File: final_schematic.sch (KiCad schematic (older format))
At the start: 50 parts, among them J1 BB_COM_Conn_01x04_Male, J2 BB_CTRL_Conn_01x02_Male, J3 BB_ON/OFF_Conn_01x04_Male, J4 BOOT0_Conn_Male, J5 OLED_SPI_Conn_01x04_Male, J6 OLED_EN_Conn_01x02_Male, J7 Conn_ARM_JTAG_SWD_10, J8 GPS_COAX, SW1 SW_Push_SESS, SW2 SW_Push_RADIO, SW3 SW_Push_RST, U1 STM32L476VGTx, U2 MTK3339, U3 RFM95W-868S2, U4 BNO055

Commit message: schematic partial fix
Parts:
- removed J2: BB_CTRL_Conn_01x02_Male, Connector_PinHeader_1.00mm:PinHeader_1x02_P1.00mm_Vertical, symbol Connector:Conn_01x02_Male
- removed J3: BB_ON/OFF_Conn_01x04_Male, Connector_PinHeader_1.00mm:PinHeader_1x01_P1.00mm_Vertical, symbol Connector:Conn_01x01_Male
- removed J4: BOOT0_Conn_Male, Connector_PinHeader_1.00mm:PinHeader_1x01_P1.00mm_Vertical, symbol Connector:Conn_01x01_Male
- removed J7: Conn_ARM_JTAG_SWD_10, Connector_PinHeader_1.27mm:PinHeader_2x05_P1.27mm_Vertical_SMD, symbol final_schematic-rescue:Conn_ARM_JTAG_SWD_10-Connector
- removed U3: RFM95W-868S2, RF_Module:HOPERF_RFM9XW_SMD, symbol final_schematic-rescue:RFM95W-868S2-RF_AM_FM
- added J2: BB_CTRL_Conn_01x03_Male, Connector_PinHeader_1.00mm:PinHeader_1x03_P1.00mm_Vertical, symbol Connector:Conn_01x03_Male
- added J3: BB_ON/OFF_CONN_01x02_Male, Connector_PinHeader_1.00mm:PinHeader_1x02_P1.00mm_Vertical, symbol Connector:Conn_01x02_Male
- added J4: BOOT0_Conn_Male, Connector_PinHeader_1.00mm:PinHeader_1x02_P1.00mm_Vertical, symbol Connector:Conn_01x02_Male
- added J7: Conn_01x06_Male, Connector_PinHeader_1.00mm:PinHeader_1x06_P1.00mm_Vertical, symbol Connector:Conn_01x06_Male
- added R11, R12, R13: 62, Resistor_SMD:R_0603_1608Metric_Pad0.98x0.95mm_HandSolder, symbol Device:R_US
- added U3: RFM95W-915S2, RF_Module:HOPERF_RFM9XW_SMD, symbol RF_AM_FM:RFM95W-915S2
- J5: value OLED_SPI_Conn_01x04_Male -> OLED_SPI_Conn_01x06_Male
- J6: value OLED_EN_Conn_01x02_Male -> OLED_EN_Conn_01x01_Male
- R1, R2: value 48 -> 62
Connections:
- net 3V3: now also J7.1 (Pin_1), U3.13 (3.3V)
- net BB_CE: now also J2.1 (Pin_1)
- net BB_GPOUT: now also J2.2 (Pin_2)
- net BOOT0: now also J4.1 (Pin_1)
- net CS_LORA: now also U3.5 (NSS)
- net DIO0: now also U3.14 (DIO0)
- net GND: now also J2.3 (Pin_3), J3.2 (Pin_2), J4.2 (Pin_2), J7.6 (Pin_6), U3.1 (GND), U3.10 (GND), U3.8 (GND)
- net LoRa_RST: now also U3.6 (RESET)
- net NRST: now also J7.2 (Pin_2), R12.2; no longer C3.2, R5.2, SW3.1
- net SPI1_MISO: now also U3.2 (MISO)
- net SPI1_MOSI: now also U3.3 (MOSI)
- net SPI1_SCK: now also U3.4 (SCK)
- net SWCLK: now also J7.3 (Pin_3)
- net SWDIO: now also J7.4 (Pin_4)
- net SWO: now also J7.5 (Pin_5)
- net SYSOFF: now also J3.1 (Pin_1)
- net radio_btn: now also R11.2; no longer C2.2, R4.2, SW2.1
- net session_btn: now also R13.2; no longer C1.2, R3.2, SW1.1
- net at LoRa_CON_Coaxial1.1 (In): now also U3.9 (ANT)
- new net: C2.2, R11.1, R4.2, SW2.1
- new net: C3.2, R12.1, R5.2, SW3.1
- new net: C1.2, R13.1, R3.2, SW1.1
- no-connect marks 71 -> 70
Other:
- note added: "STM32 Connector"
- note removed: "JTAG Debugger/Programmer"
- moved on the sheet: C1, C2, C3, R3, R4, R5, SW1, SW2, SW3

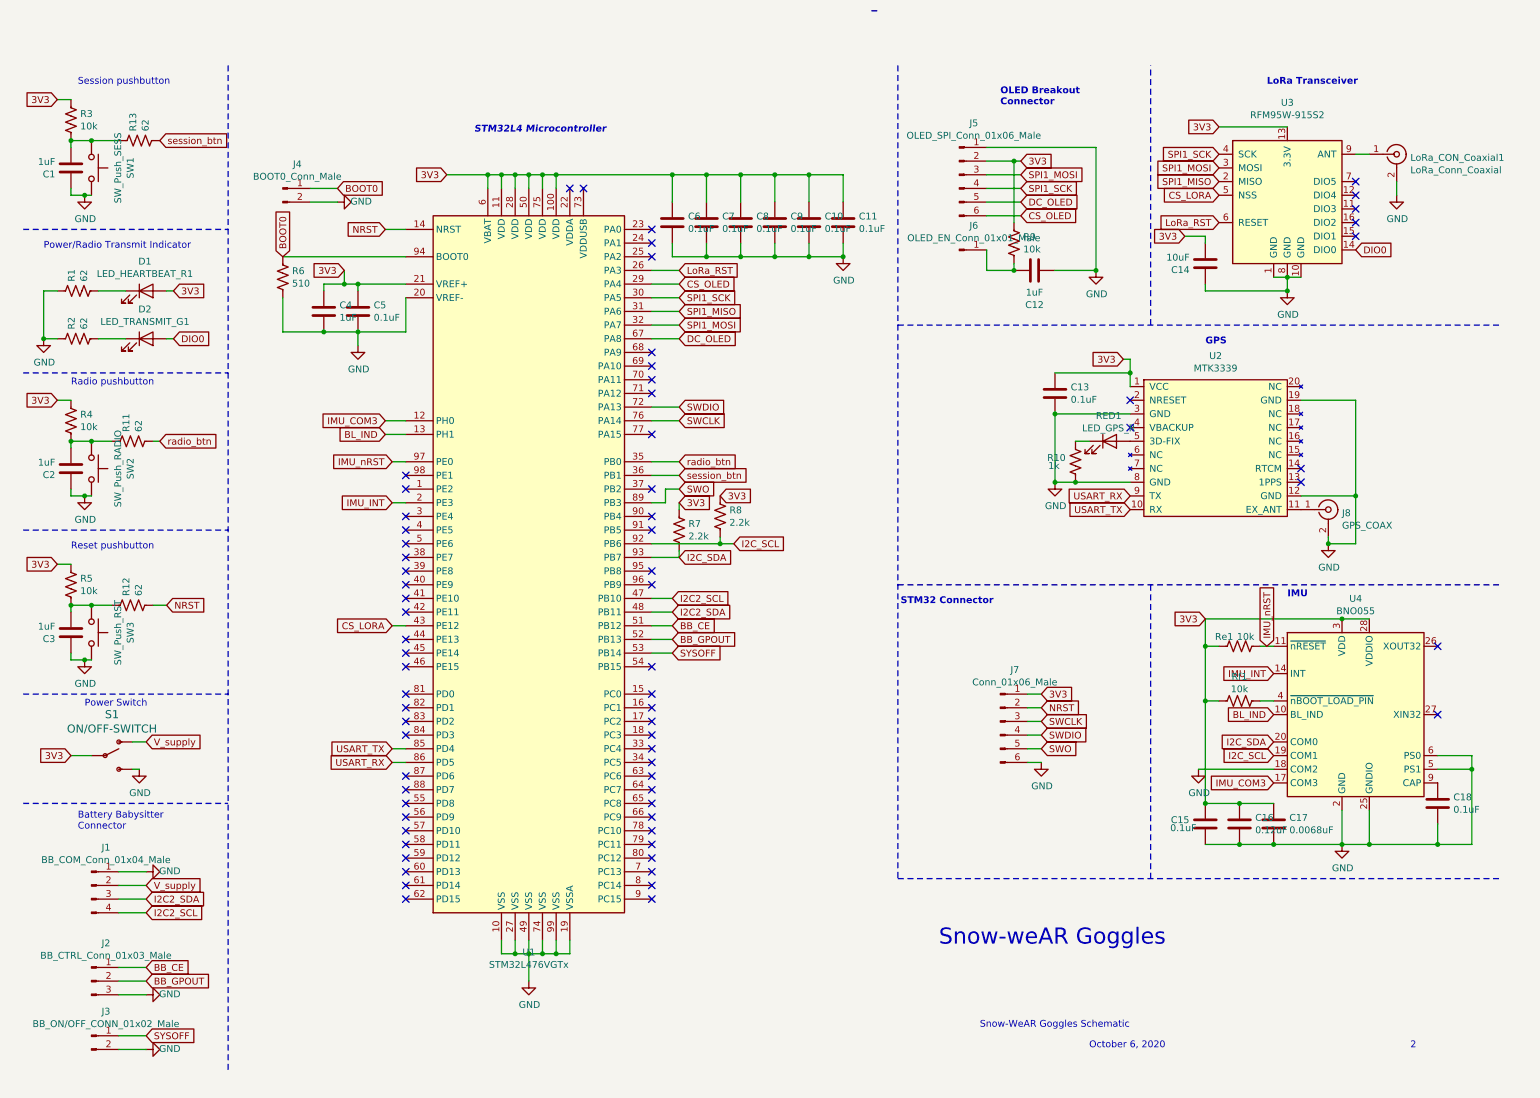
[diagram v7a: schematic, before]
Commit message: added voltage regulator because we need it
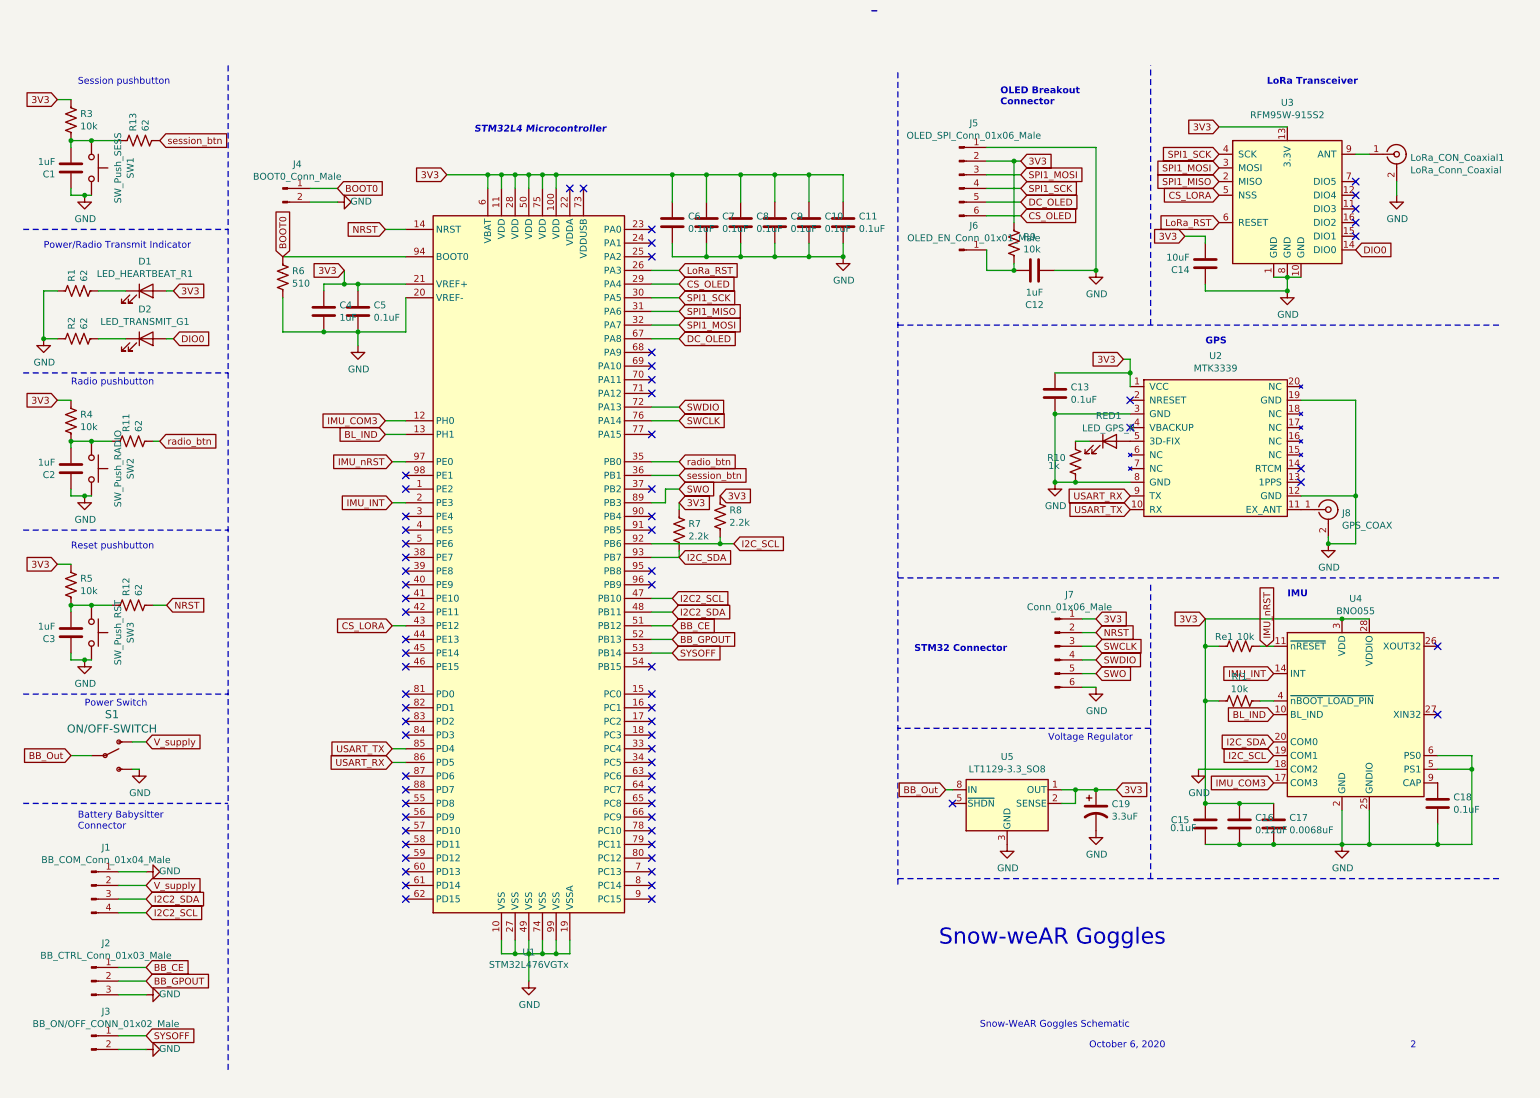
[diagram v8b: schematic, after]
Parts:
- added C19: 3.3uF, Capacitor_Tantalum_SMD:CP_EIA-7343-15_Kemet-W_Pad2.25x2.55mm_HandSolder, symbol Device:CP1
- added U5: LT1129-3.3_SO8, Package_SO:SOIC-8_3.9x4.9mm_P1.27mm, symbol Regulator_Linear:LT1129-3.3_SO8
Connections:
- net 3V3: now also C19.1, U5.1 (OUT), U5.2 (SENSE); no longer S1.2 (P)
- net GND: now also C19.2, U5.3 (GND), U5.6 (GND), U5.7 (GND)
- new net BB_Out: S1.2 (P), U5.8 (IN)
- no-connect marks 70 -> 71
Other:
- note added: "Voltage Regulator"
- moved on the sheet: J7
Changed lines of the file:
@@
 Text Notes 7150 6900 0    118  ~ 0
 Snow-weAR Goggles\n
-Text GLabel 7900 5350 2    50   Input ~ 0
+Text GLabel 8300 4800 2    50   Input ~ 0
 SWDIO
-Text GLabel 7900 5250 2    50   Input ~ 0
+Text GLabel 8300 4700 2    50   Input ~ 0
 SWCLK
-Text GLabel 7900 5050 2    50   Input ~ 0
+Text GLabel 8300 4500 2    50   Input ~ 0
 3V3
 Wire Wire Line
-	7900 5350 7800 5350
-Text GLabel 7900 5150 2    50   Input ~ 0
+	8300 4800 8200 4800
+Text GLabel 8300 4600 2    50   Input ~ 0
 NRST
 Wire Wire Line
-	7900 5150 7800 5150
-Text GLabel 7900 5450 2    50   Input ~ 0
+	8300 4600 8200 4600
+Text GLabel 8300 4900 2    50   Input ~ 0
 SWO
 Wire Wire Line
-	7900 5450 7800 5450
+	8300 4900 8200 4900
 $Comp
 L Connector:Conn_01x04_Male J1
@@
 Wire Wire Line
 	1350 6650 1150 6650
-Text Notes 7550 4400 2    50   ~ 10
-STM32 Connector
 Wire Wire Line
 	10000 3950 10200 3950
@@
 L power:GND #PWR010
 U 1 1 60380C60
-P 7900 5550
-F 0 "#PWR010" H 7900 5300 50  0001 C CNN
-F 1 "GND" H 7905 5377 50  0000 C CNN
-F 2 "" H 7900 5550 50  0001 C CNN
-F 3 "" H 7900 5550 50  0001 C CNN
-	1    7900 5550
+P 8300 5000
+F 0 "#PWR010" H 8300 4750 50  0001 C CNN
+F 1 "GND" H 8305 4827 50  0000 C CNN
+F 2 "" H 8300 5000 50  0001 C CNN
+F 3 "" H 8300 5000 50  0001 C CNN
+	1    8300 5000
 	1    0    0    -1
 $EndComp
@@
 V_supply
 Text GLabel 800  5500 0    50   Input ~ 0
-3V3
+BB_Out
 Wire Wire Line
 	800  5500 950  5500
@@
 NoConn ~ 10200 1700
 Wire Wire Line
-	7900 5250 7800 5250
+	8300 4700 8200 4700
 $Comp
 L power:GND #PWR016
@@
 Connection ~ 7700 1950
 Wire Wire Line
-	7900 5550 7800 5550
+	8300 5000 8200 5000
 NoConn ~ 9800 3400
 NoConn ~ 9800 3500
@@
 STM32L4 Microcontroller
 Wire Notes Line
-	6850 450  6850 6400
-Wire Notes Line
 	6850 2350 11250 2350
 Wire Notes Line
-	6850 4250 11250 4250
+	6850 4200 11250 4200
 Wire Notes Line
 	6850 6400 11250 6400
@@
 L Connector:Conn_01x06_Male J7
 U 1 1 5FADFDD2
-P 7600 5250
-F 0 "J7" H 7706 5628 50  0000 C CNN
-F 1 "Conn_01x06_Male" H 7706 5537 50  0000 C CNN
-F 2 "Connector_PinHeader_1.00mm:PinHeader_1x06_P1.00mm_Vertical" H 7600 5250 50  0001 C CNN
-F 3 "~" H 7600 5250 50  0001 C CNN
-	1    7600 5250
-	1    0    0    -1
-$EndComp
-Wire Wire Line
-	7900 5050 7800 5050
+P 8000 4700
+F 0 "J7" H 8106 5078 50  0000 C CNN
+F 1 "Conn_01x06_Male" H 8106 4987 50  0000 C CNN
+F 2 "Connector_PinHeader_1.00mm:PinHeader_1x06_P1.00mm_Vertical" H 8000 4700 50  0001 C CNN
+F 3 "~" H 8000 4700 50  0001 C CNN
+	1    8000 4700
+	1    0    0    -1
+$EndComp
+Wire Wire Line
+	8300 4500 8200 4500
 Wire Wire Line
 	950  1000 1150 1000
+$Comp
+L Regulator_Linear:LT1129-3.3_SO8 U5
+U 1 1 5FC4BDF4
+P 7650 5850
+F 0 "U5" H 7650 6192 50  0000 C CNN
+F 1 "LT1129-3.3_SO8" H 7650 6101 50  0000 C CNN
+F 2 "Package_SO:SOIC-8_3.9x4.9mm_P1.27mm" H 7650 6150 50  0001 C CNN
+F 3 "http://cds.linear.com/docs/en/datasheet/112935ff.pdf" H 7650 5850 50  0001 C CNN
+	1    7650 5850
+	1    0    0    -1
+$EndComp
+$Comp
+L Device:CP1 C19
+U 1 1 5FC4C1D2
+P 8300 5900
+F 0 "C19" H 8415 5946 50  0000 L CNN
+F 1 "3.3uF" H 8415 5855 50  0000 L CNN
+F 2 "Capacitor_Tantalum_SMD:CP_EIA-7343-15_Kemet-W_Pad2.25x2.55mm_HandSolder" H 8300 5900 50  0001 C CNN
+F 3 "~" H 8300 5900 50  0001 C CNN
+	1    8300 5900
+	1    0    0    -1
+$EndComp
+$Comp
+L power:GND #PWR019
+U 1 1 5FC4C2FA
+P 8300 6050
+F 0 "#PWR019" H 8300 5800 50  0001 C CNN
+F 1 "GND" H 8305 5877 50  0000 C CNN
+F 2 "" H 8300 6050 50  0001 C CNN
+F 3 "" H 8300 6050 50  0001 C CNN
+	1    8300 6050
+	1    0    0    -1
+$EndComp
+NoConn ~ 7250 5850
+Text GLabel 7200 5750 0    50   Input ~ 0
+BB_Out
+Text GLabel 8450 5750 2    50   Input ~ 0
+3V3
+Wire Wire Line
+	8450 5750 8300 5750
+Connection ~ 8300 5750
+Wire Wire Line
+	8300 5750 8150 5750
+Wire Wire Line
+	8050 5850 8150 5850
+Wire Wire Line
+	8150 5850 8150 5750
+Connection ~ 8150 5750
+Wire Wire Line
+	8150 5750 8050 5750
+$Comp
+L power:GND #PWR018
+U 1 1 5FC75E8F
+P 7650 6150
+F 0 "#PWR018" H 7650 5900 50  0001 C CNN
+F 1 "GND" H 7655 5977 50  0000 C CNN
+F 2 "" H 7650 6150 50  0001 C CNN
+F 3 "" H 7650 6150 50  0001 C CNN
+	1    7650 6150
+	1    0    0    -1
+$EndComp
+Wire Wire Line
+	7250 5750 7200 5750
+Text Notes 7650 4750 2    50   ~ 10
+STM32 Connector
+Wire Notes Line
+	8700 5300 6850 5300
+Wire Notes Line
+	6850 500  6850 6450
+Text Notes 7950 5400 0    50   ~ 0
+Voltage Regulator
 $EndSCHEMATC
